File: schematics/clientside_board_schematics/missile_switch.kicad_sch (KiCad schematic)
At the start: 28 parts, among them J11 MV2 Connector, J12 MV1 Connector, J13 MV3 Connector, J14 MV4 Connector, J15 MV5 Connector, J16 MV6 Connector, J17 MV7 Connector, J18 MV8 Connector, J19 ARM_PRI Connector, J20 ARM_SEC Connector, J21 INJ Connector, J3 Missile Switch Light Ground, Q1 PJA3405, Q2 TSM2306CX

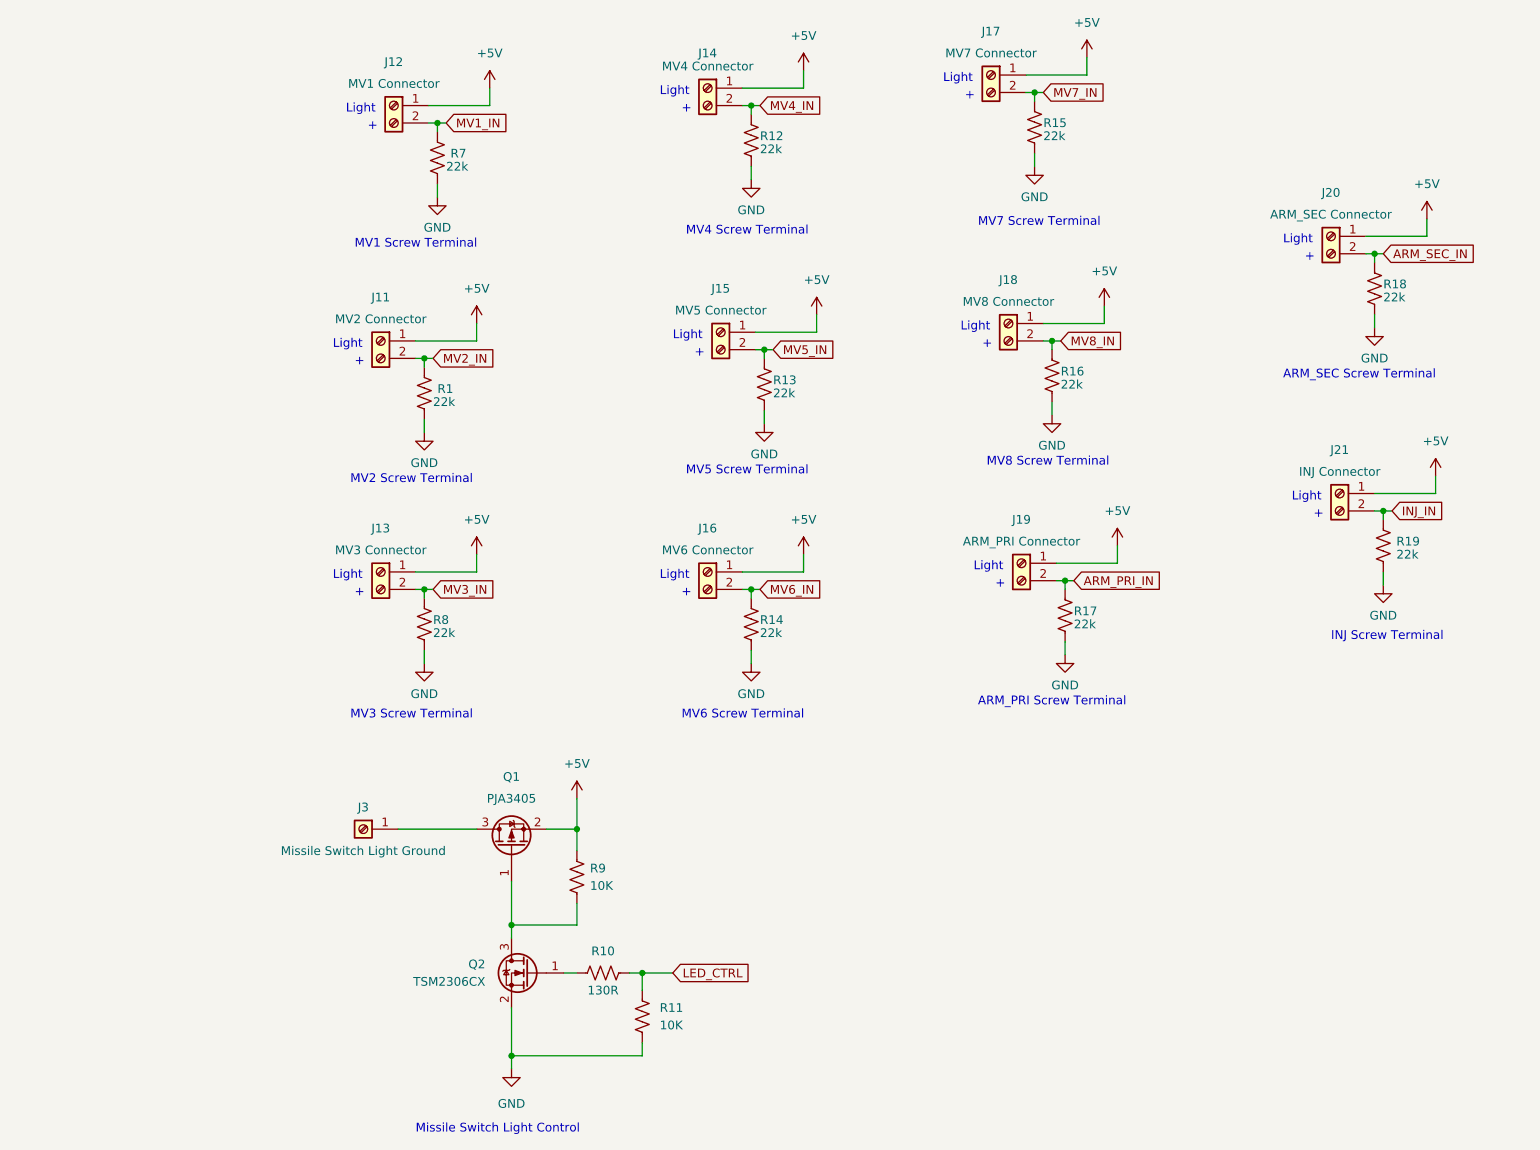
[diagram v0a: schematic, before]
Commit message: Update client-side board schematic
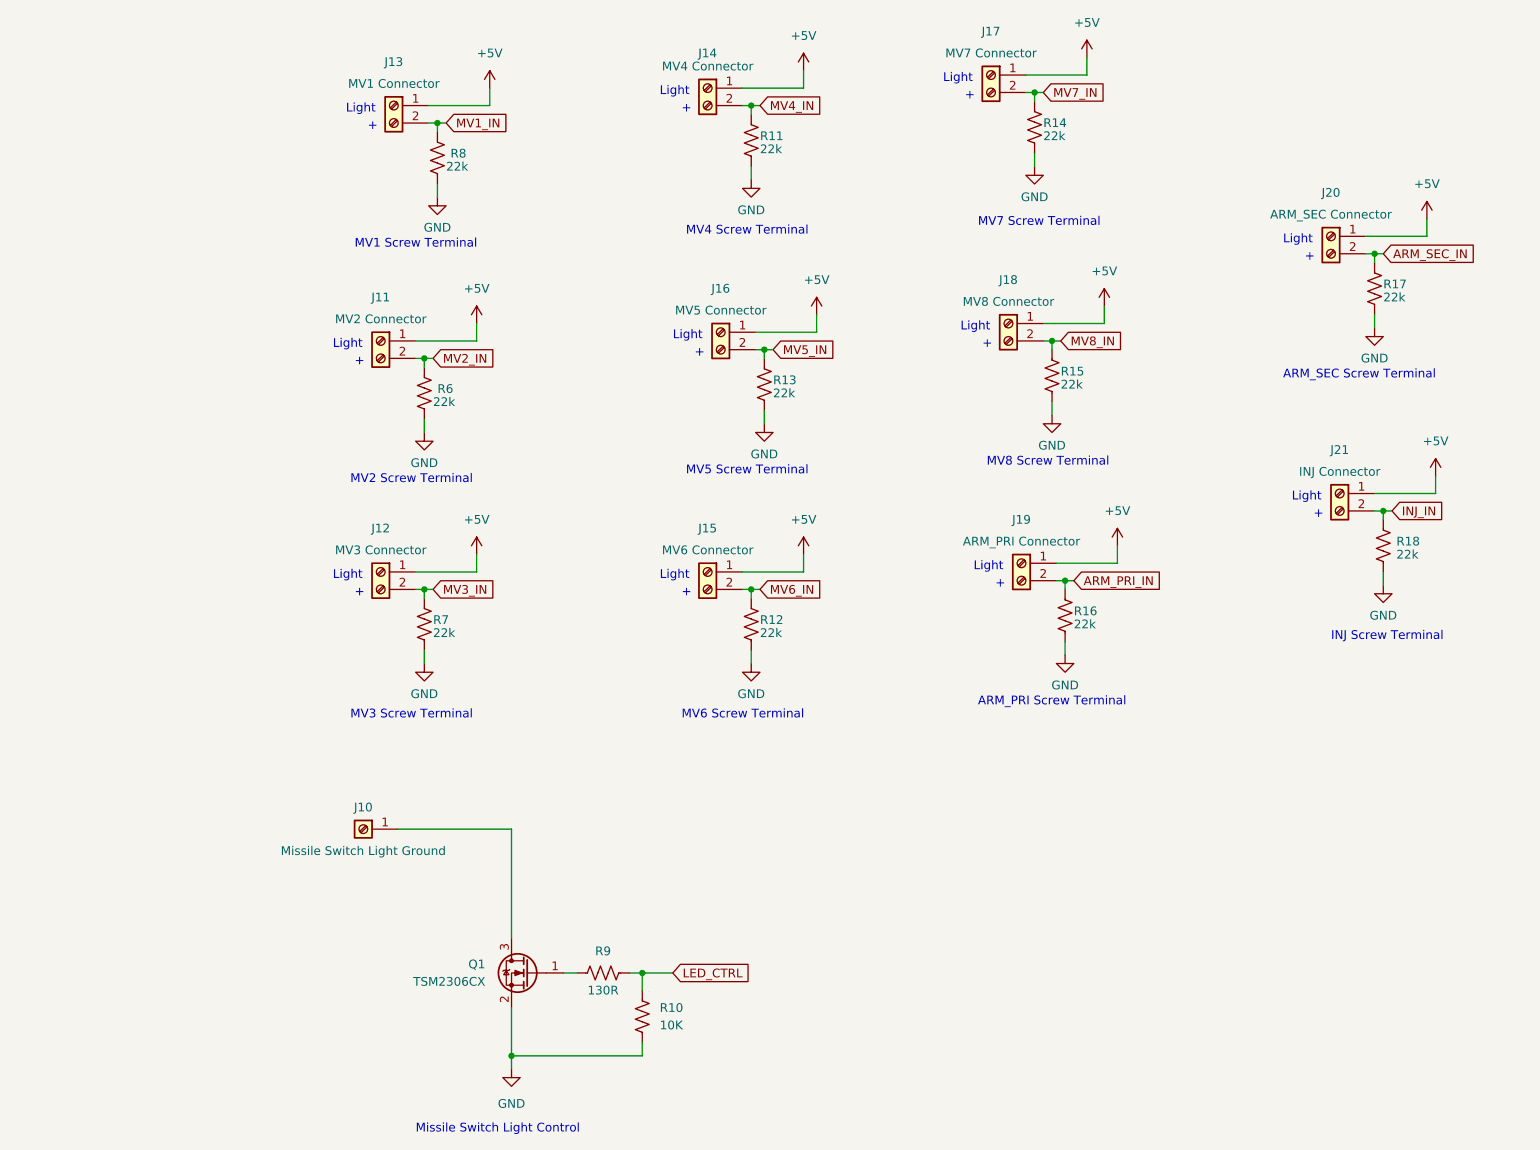
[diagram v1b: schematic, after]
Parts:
- removed Q1: PJA3405, Package_TO_SOT_SMD:SOT-23_Handsoldering, symbol Device:Q_PMOS_GSD
- removed R9: 10K, Resistor_SMD:R_0805_2012Metric_Pad1.20x1.40mm_HandSolder, symbol Device:R_US
- renumbered J3 to J10, J13 to J12, J12 to J13, J16 to J15, J15 to J16, Q2 to Q1, R11 to R10, R12 to R11, R14 to R12, R15 to R14, R16 to R15, R17 to R16, R18 to R17, R19 to R18, R1 to R6, R8 to R7, R7 to R8, R10 to R9
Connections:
- net at Q1.3 (D): now also J10.1 (Pin_1)

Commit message: Update Client-side board schematic for reduce routing complexity
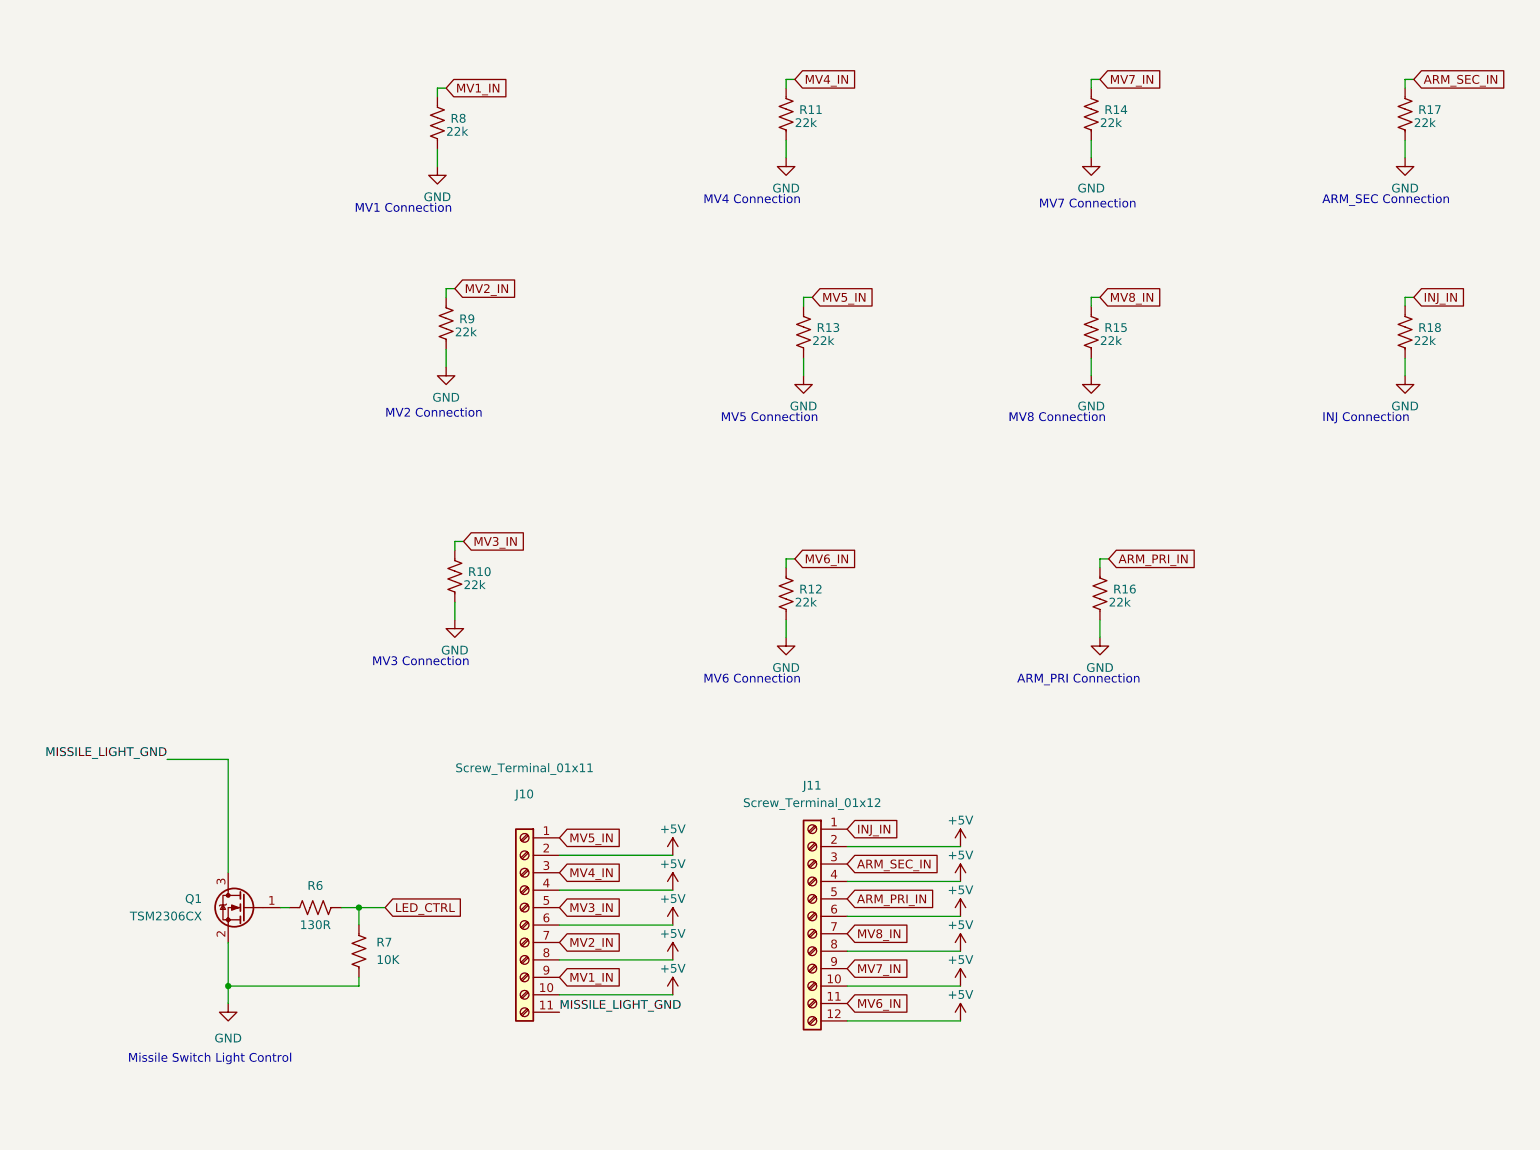
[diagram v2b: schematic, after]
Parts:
- removed J10: Missile Switch Light Ground, TerminalBlock_Phoenix:TerminalBlock_Phoenix_PT-1,5-2-3.5-H_1x02_P3.50mm_Horizontal, symbol Connector:Screw_Terminal_01x01
- removed J11: MV2 Connector, TerminalBlock_Phoenix:TerminalBlock_Phoenix_PT-1,5-2-3.5-H_1x02_P3.50mm_Horizontal, symbol Connector:Screw_Terminal_01x02
- removed J12: MV3 Connector, TerminalBlock_Phoenix:TerminalBlock_Phoenix_PT-1,5-2-3.5-H_1x02_P3.50mm_Horizontal, symbol Connector:Screw_Terminal_01x02
- removed J13: MV1 Connector, TerminalBlock_Phoenix:TerminalBlock_Phoenix_PT-1,5-2-3.5-H_1x02_P3.50mm_Horizontal, symbol Connector:Screw_Terminal_01x02
- removed J14: MV4 Connector, TerminalBlock_Phoenix:TerminalBlock_Phoenix_PT-1,5-2-3.5-H_1x02_P3.50mm_Horizontal, symbol Connector:Screw_Terminal_01x02
- removed J15: MV6 Connector, TerminalBlock_Phoenix:TerminalBlock_Phoenix_PT-1,5-2-3.5-H_1x02_P3.50mm_Horizontal, symbol Connector:Screw_Terminal_01x02
- removed J16: MV5 Connector, TerminalBlock_Phoenix:TerminalBlock_Phoenix_PT-1,5-2-3.5-H_1x02_P3.50mm_Horizontal, symbol Connector:Screw_Terminal_01x02
- removed J17: MV7 Connector, TerminalBlock_Phoenix:TerminalBlock_Phoenix_PT-1,5-2-3.5-H_1x02_P3.50mm_Horizontal, symbol Connector:Screw_Terminal_01x02
- removed J18: MV8 Connector, TerminalBlock_Phoenix:TerminalBlock_Phoenix_PT-1,5-2-3.5-H_1x02_P3.50mm_Horizontal, symbol Connector:Screw_Terminal_01x02
- removed J19: ARM_PRI Connector, TerminalBlock_Phoenix:TerminalBlock_Phoenix_PT-1,5-2-3.5-H_1x02_P3.50mm_Horizontal, symbol Connector:Screw_Terminal_01x02
- removed J20: ARM_SEC Connector, TerminalBlock_Phoenix:TerminalBlock_Phoenix_PT-1,5-2-3.5-H_1x02_P3.50mm_Horizontal, symbol Connector:Screw_Terminal_01x02
- removed J21: INJ Connector, TerminalBlock_Phoenix:TerminalBlock_Phoenix_PT-1,5-2-3.5-H_1x02_P3.50mm_Horizontal, symbol Connector:Screw_Terminal_01x02
- removed R6, R7: 22k, Resistor_SMD:R_0805_2012Metric_Pad1.20x1.40mm_HandSolder, symbol Device:R_US
- added J10: Screw_Terminal_01x11, TerminalBlock_Phoenix:TerminalBlock_Phoenix_PT-1,5-11-3.5-H_1x11_P3.50mm_Horizontal, symbol Connector:Screw_Terminal_01x11
- added J11: Screw_Terminal_01x12, TerminalBlock_Phoenix:TerminalBlock_Phoenix_PT-1,5-12-3.5-H_1x12_P3.50mm_Horizontal, symbol Connector:Screw_Terminal_01x12
- added R10, R9: 22k, Resistor_SMD:R_0805_2012Metric_Pad1.20x1.40mm_HandSolder, symbol Device:R_US
- renumbered R9 to R6, R10 to R7
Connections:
- net +5V: now also J10.10 (Pin_10), J10.2 (Pin_2), J10.4 (Pin_4), J10.6 (Pin_6), J10.8 (Pin_8), J11.10 (Pin_10), J11.12 (Pin_12), J11.2 (Pin_2), J11.4 (Pin_4), J11.6 (Pin_6), J11.8 (Pin_8)
- net ARM_PRI_IN: now also J11.5 (Pin_5)
- net ARM_SEC_IN: now also J11.3 (Pin_3)
- net GND: now also R10.2, R9.2
- net INJ_IN: now also J11.1 (Pin_1)
- net MV1_IN: now also J10.9 (Pin_9)
- net MV2_IN: now also J10.7 (Pin_7), R9.1
- net MV3_IN: now also J10.5 (Pin_5), R10.1
- net MV4_IN: now also J10.3 (Pin_3)
- net MV5_IN: now also J10.1 (Pin_1)
- net MV6_IN: now also J11.11 (Pin_11)
- net MV7_IN: now also J11.9 (Pin_9)
- net MV8_IN: now also J11.7 (Pin_7)
- net MISSILE_LIGHT_GND: now reaches Q1.3 (D)
- net MISSILE_LIGHT_GND: now also J10.11 (Pin_11)
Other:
- note added: "ARM_PRI Connection"
- note added: "ARM_SEC Connection"
- note added: "INJ Connection"
- note added: "MV1 Connection"
- note added: "MV2 Connection"
- note added: "MV3 Connection"
- note added: "MV4 Connection"
- note added: "MV5 Connection"
- note added: "MV6 Connection"
- note added: "MV7 Connection"
- note added: "MV8 Connection"
- note removed: "+"
- note removed: "ARM_PRI Screw Terminal"
- note removed: "ARM_SEC Screw Terminal"
- note removed: "INJ Screw Terminal"
- note removed: "Light"
- note removed: "MV1 Screw Terminal"
- note removed: "MV2 Screw Terminal"
- note removed: "MV3 Screw Terminal"
- note removed: "MV4 Screw Terminal"
- note removed: "MV5 Screw Terminal"
- note removed: "MV6 Screw Terminal"
- note removed: "MV7 Screw Terminal"
- note removed: "MV8 Screw Terminal"
- moved on the sheet: Q1, R6, R7, R8

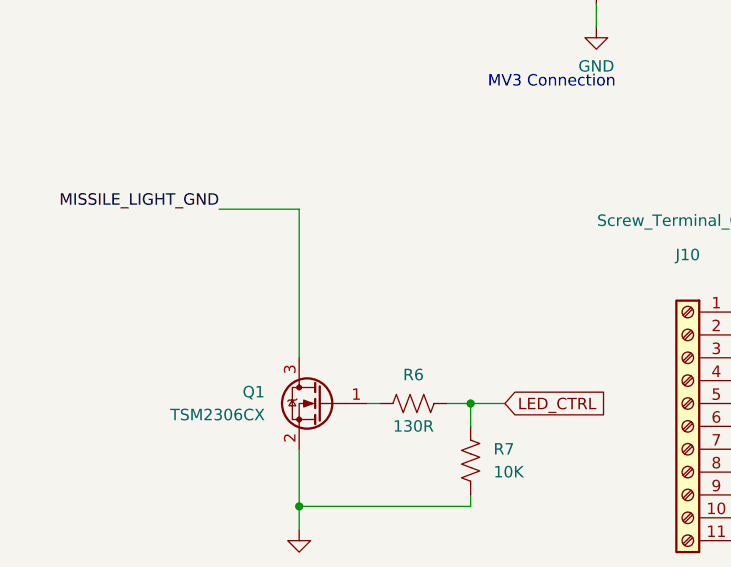
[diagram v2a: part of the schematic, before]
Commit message: Add name to client-side board silkscreen
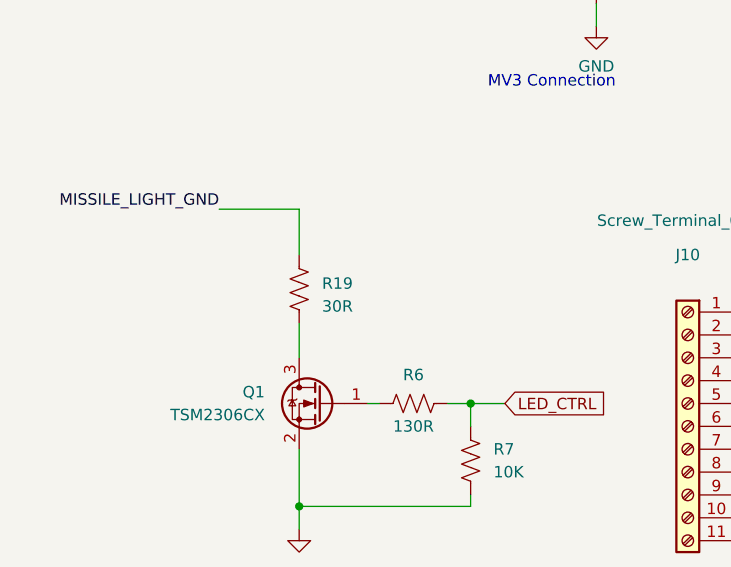
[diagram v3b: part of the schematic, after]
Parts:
- added R19: 30R, Resistor_SMD:R_0805_2012Metric_Pad1.20x1.40mm_HandSolder, symbol Device:R_US
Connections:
- net MISSILE_LIGHT_GND: now also R19.1; no longer Q1.3 (D)
- new net: Q1.3 (D), R19.2
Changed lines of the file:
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@@
   (junction (at 60.96 161.29) (diameter 0) (color 0 0 0 0)
   )
+  (wire (pts (xy 60.96 140.97) (xy 60.96 144.78))
+    (stroke (width 0) (type default))
+  )
   (wire (pts (xy 80.01 149.86) (xy 80.01 152.4))
     (stroke (width 0) (type default))
@@
     (stroke (width 0) (type default))
   )
-  (wire (pts (xy 60.96 128.27) (xy 60.96 144.78))
-    (stroke (width 0) (type default))
-  )
   (wire (pts (xy 92.71 59.69) (xy 93.98 59.69))
     (stroke (width 0) (type default))
@@
   )
   (wire (pts (xy 109.22 147.32) (xy 125.73 147.32))
+    (stroke (width 0) (type default))
+  )
+  (wire (pts (xy 60.96 128.27) (xy 60.96 133.35))
     (stroke (width 0) (type default))
   )
@@
         )
       )
+    )
+  )
+  (symbol (lib_id "Device:R_US") (at 60.96 137.16 0) (unit 1)
+    (in_bom yes) (on_board yes) (dnp no) (fields_autoplaced)
+    (property "Reference" "R19" (at 63.5 136.525 0)
+      (effects (font (size 1.27 1.27)) (justify left))
+    )
+    (property "Value" "30R" (at 63.5 139.065 0)
+      (effects (font (size 1.27 1.27)) (justify left))
+    )
+    (property "Footprint" "Resistor_SMD:R_0805_2012Metric_Pad1.20x1.40mm_HandSolder" (at 61.976 137.414 90)
+      (effects (font (size 1.27 1.27)) hide)
+    )
+    (property "Datasheet" "~" (at 60.96 137.16 0)
+      (effects (font (size 1.27 1.27)) hide)
+    )
+    (pin "1")
+    (pin "2")
+    (instances
+      (project "clientside_board_schematics"
+        (path "/e26fd3bf-cce6-4c8d-bab3-b3c9711619ce/b60a76b7-a357-4c64-85bd-07c83ac8458d"
+          (reference "R19") (unit 1)
+        )
+      )
